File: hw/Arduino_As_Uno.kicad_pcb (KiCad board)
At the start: 2 copper layers, 68.6 x 53.3 mm, 170 parts, among them CON1 BARREL_JACK, P1 USB_OTG, P10 CONN_01X06, P11 CONN_01X08, P13 CONN_02X03, P14 CONN_02X03_ICSP, P15 CONN_01X08, P2 CONN_02X03_ICSP, P22 CONN_02X03_ICSP, P3 CONN_02X03, P4 CONN_02X03_ICSP, P5 CONN_01X08, P6 CONN_02X03, P7 CONN_02X03_ICSP, P8 CONN_02X03_ICSP, P9 CONN_01X10, Q1 FDN340P, SW1 SW_PUSH, U1 LM2940LD-5.0, U10 TS3A44159, U11 FDG6331L, U2 MIC5205, U3 ATMEGA16U2, U4 23K256, U5 ATTINY85-SUR, U6 TS3A44159, U7 ATMEGA328PB-MU, U8 74LVCH1T45, U9 ATTINY85-SUR, X1 CRYSTAL, X2 RESONATOR

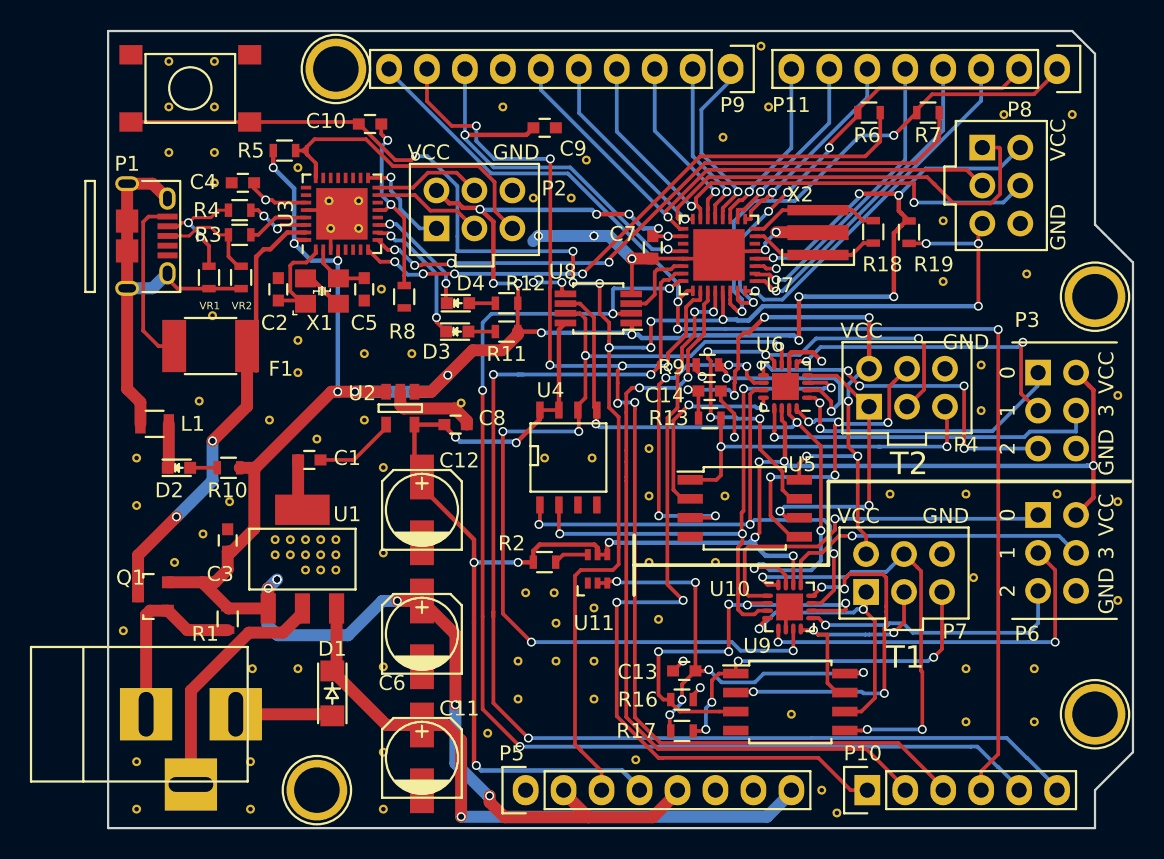
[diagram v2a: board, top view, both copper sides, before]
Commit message: Completed routing.. Macrofab requires a 1.6mm clearance on traces. I made everything with 1.5mm. I'll be back.
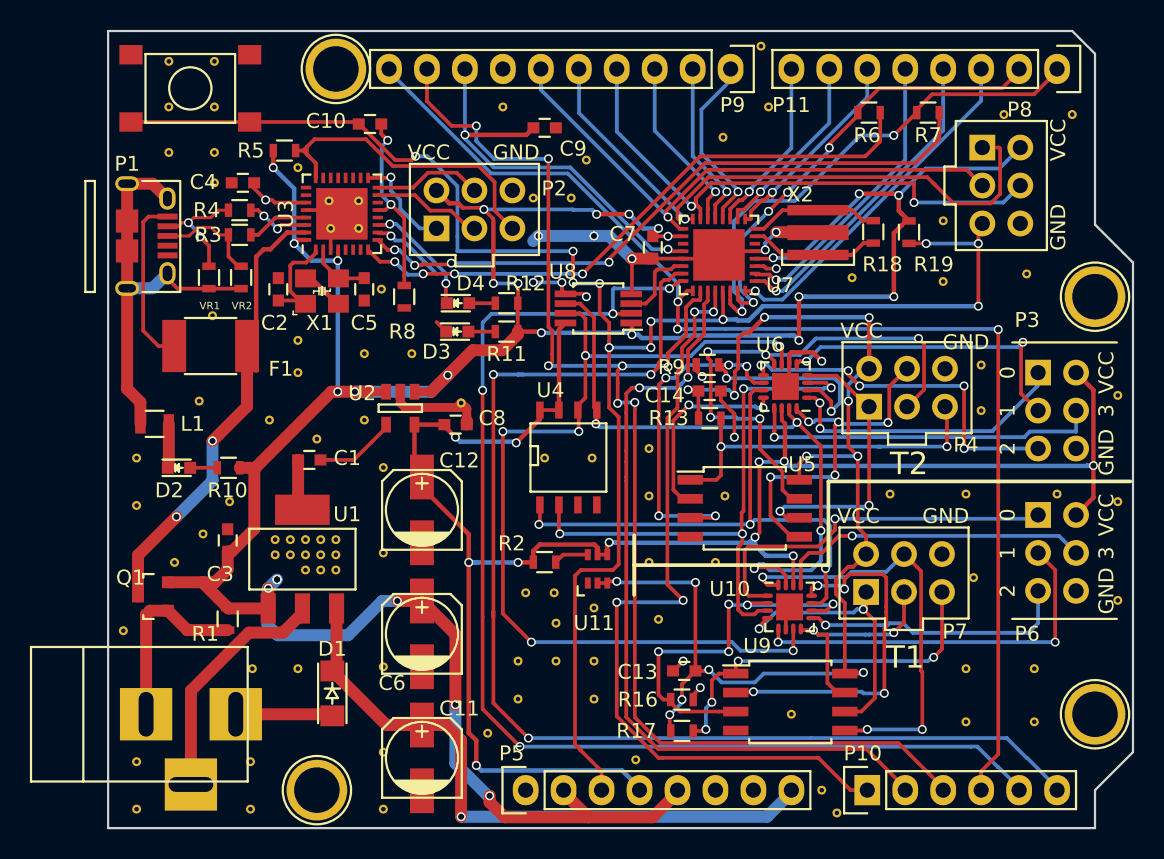
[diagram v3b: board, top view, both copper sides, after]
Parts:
- added REF**: stitchingVIA, pcbfp_lib:via_.3, F.Cu at (160.8, 89.5)
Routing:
- net /3.3V_UNSAFE: track 73.7 -> 83.0 mm
- net /RXLED: track 9.20 -> 5.98 mm, vias 2 -> 1
- net GND: track 76.8 -> 79.9 mm, vias 12 -> 13
- net /SELECT_T2: track 28.6 -> 26.6 mm
- net +3V3: track 122.7 -> 123.4 mm
- net /~SS~_T2: track 24.0 -> 24.6 mm
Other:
- net class Default: clearance 0.15 -> 0.16
- rule trace_clearance: 0.15 -> 0.16
- board text added: "thimble.io 2016"

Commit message: Completed PCB layout.
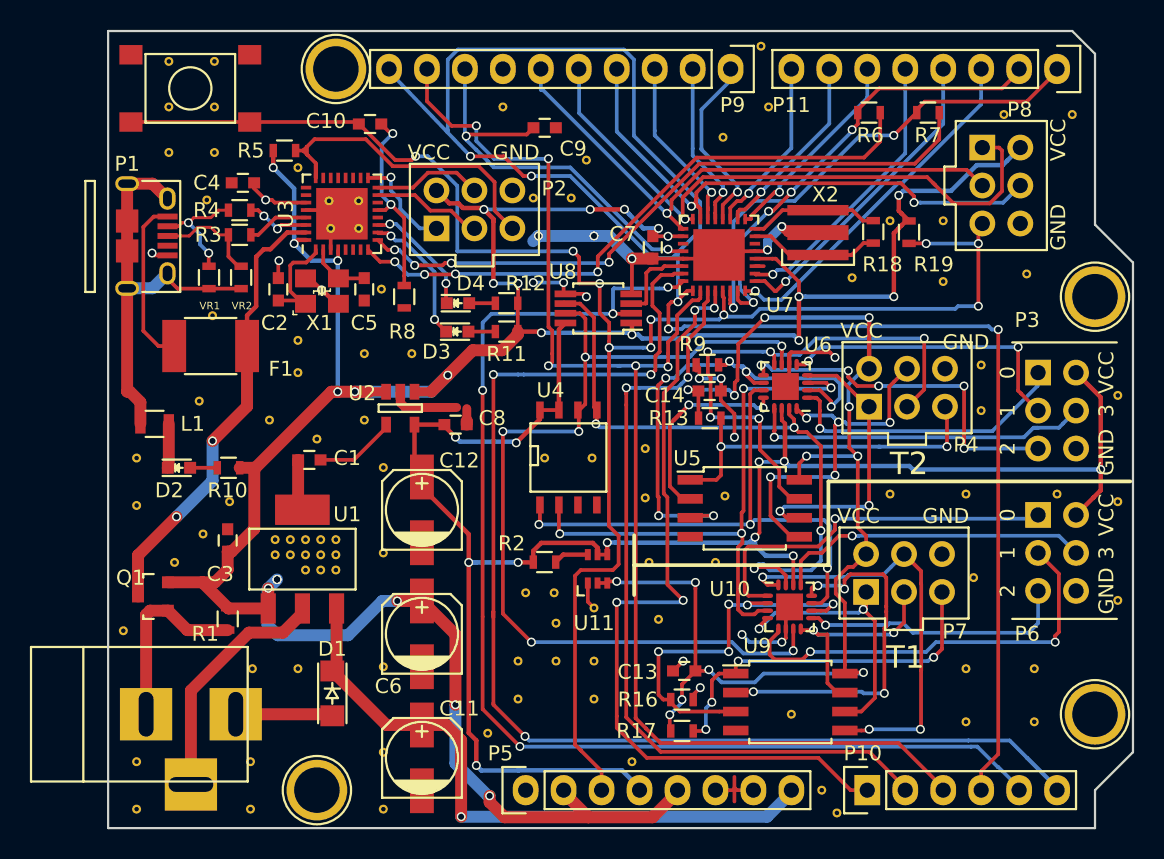
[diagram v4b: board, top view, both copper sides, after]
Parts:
- moved REF** 31.2 mm to (163.3, 85.7)
- moved REF** 1.25 mm to (117.6, 84.3)
- moved REF** 0.28 mm to (146.9, 104.3)
- moved REF** 0.28 mm to (146.1, 121.9)
- moved REF** 0.25 mm to (146.9, 101.0)
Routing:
- net /AD3/SCL: track 83.2 -> 119.3 mm, vias 3 -> 5
- net GND: track 79.9 -> 94.7 mm, vias 13 -> 19
- net +5V: track 200.3 -> 193.5 mm, vias 27 -> 25
- net /AD5/MISO1: track 81.8 -> 85.1 mm
- net /RXLED: track 5.98 -> 9.20 mm, vias 1 -> 2
- net /IO1_T2: track 25.9 -> 28.3 mm
- net /SELECT_T1: track 36.9 -> 34.6 mm, vias 7 -> 6
- net /RES1_328: track 10.5 -> 8.77 mm
- net /~SS~_T1: track 13.2 -> 14.8 mm
- net +3V3: track 123.4 -> 124.9 mm
- net /USBVCC: track 31.4 -> 30.0 mm
- net /AD2/SDA: track 88.6 -> 87.3 mm, vias 7 -> 5
- net /IO0/RX: track 34.2 -> 33.1 mm
- net Net-(U7-Pad3): track 1.50 -> 0.60 mm, vias 1 -> 0
- net /SCK_RAM: track 63.3 -> 64.2 mm
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
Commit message: Pre-production commit. Silkscreen added and some designators moved away from vias. Added BOM/picknplace
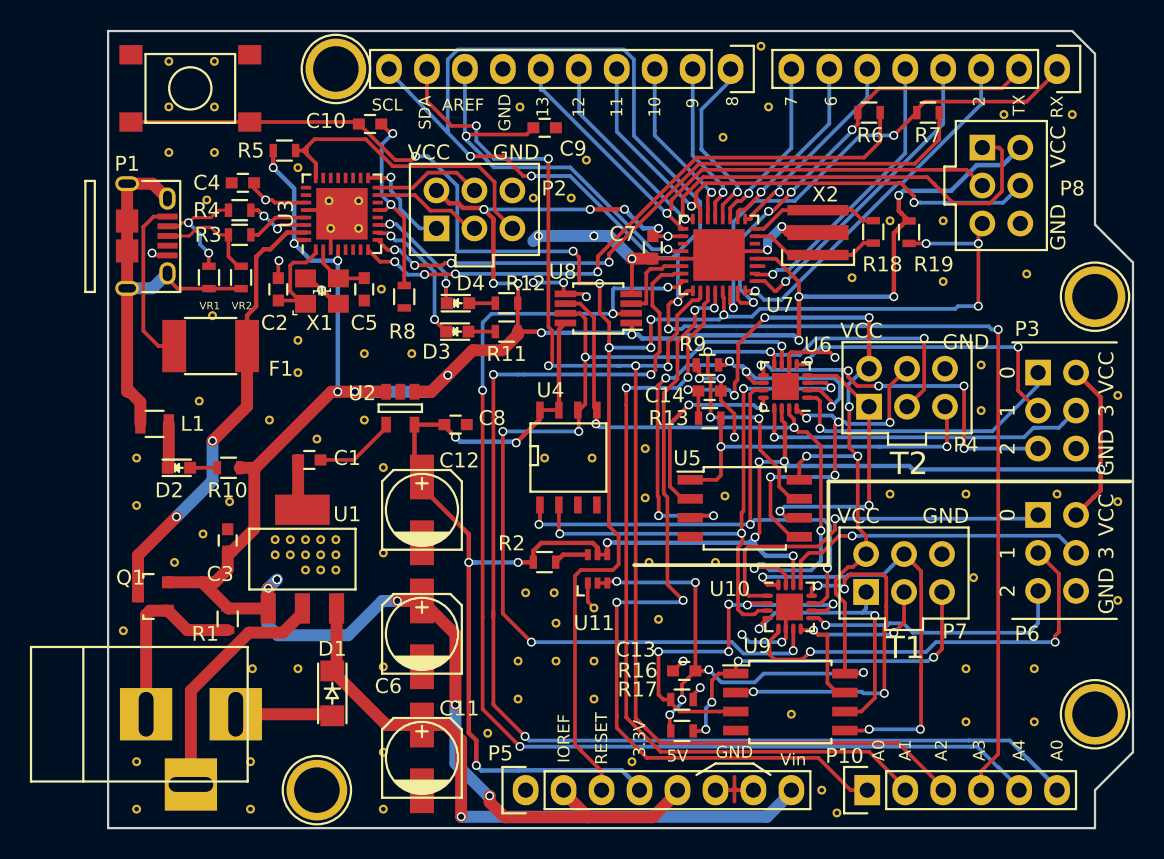
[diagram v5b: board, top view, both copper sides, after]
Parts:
- moved REF** 1.14 mm to (138.6, 78.1)
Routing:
- net GND: track 94.7 -> 88.7 mm
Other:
- board text added: "10"
- board text added: "11"
- board text added: "12"
- board text added: "13"
- board text added: "2"
- board text added: "3.3V"
- board text added: "5V"
- board text added: "6"
- board text added: "7"
- board text added: "8"
- board text added: "9"
- board text added: "A0"
- board text added: "A1"
- board text added: "A2"
- board text added: "A3"
- board text added: "A4"
- board text added: "AREF"
- board text added: "GND"
- board text added: "IOREF"
- board text added: "RESET"
- board text added: "RX"
- board text added: "SCL"
- board text added: "SDA"
- board text added: "TX"
- board text added: "Vin"
